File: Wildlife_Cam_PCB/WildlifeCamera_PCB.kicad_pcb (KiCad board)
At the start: 2 copper layers, 79.8 x 84.8 mm, 46 parts, among them J1 PIR, J2 TRIG, J3 RTC_DS3231, J4 PROG, J5 PROG_EN, J6 LOGO1, J7 LOGO2, J8 PCB, Q1 2N3904, Q2 2N3904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

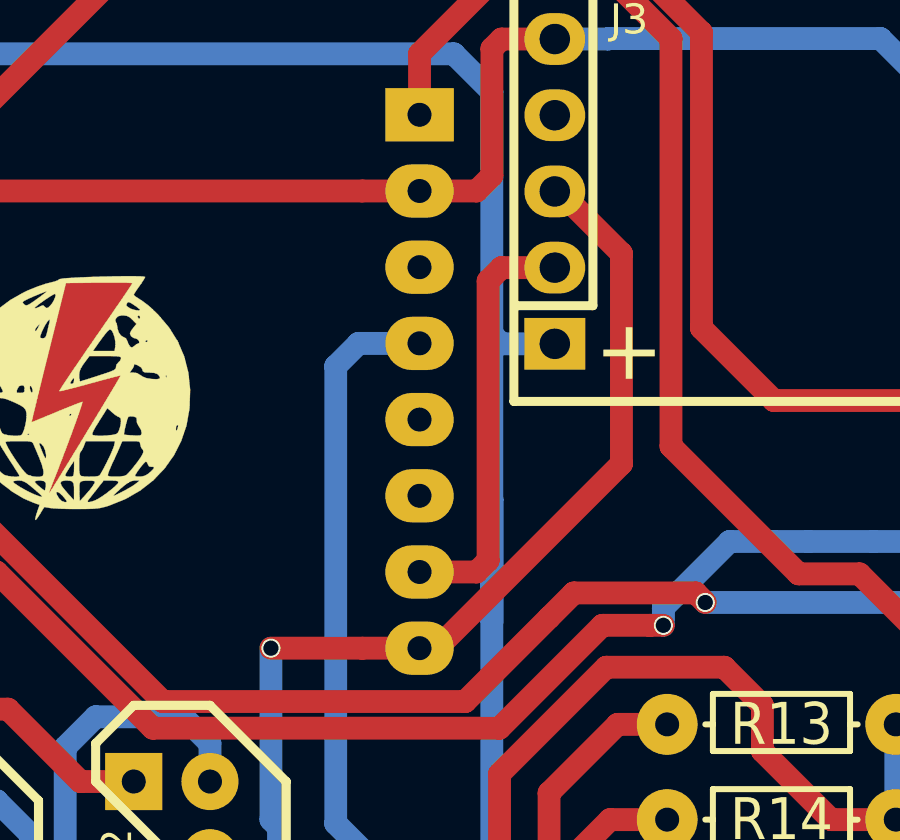
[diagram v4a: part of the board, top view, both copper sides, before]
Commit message: Large update with email sending code
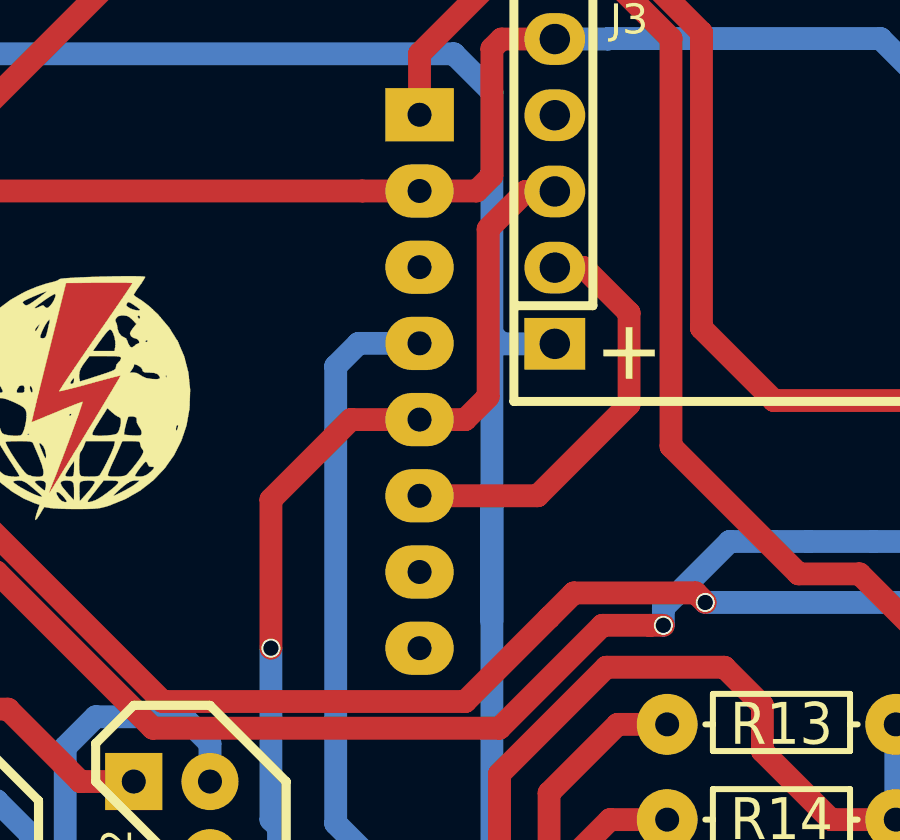
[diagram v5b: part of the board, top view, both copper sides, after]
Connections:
- U3 pad 5: Net-(U3-Pad5) -> /I2C_CLK
- U3 pad 6: Net-(U3-Pad6) -> /I2C_DAT
- U3 pad 7: /I2C_DAT -> Net-(U3-Pad7)
- U3 pad 8: /I2C_CLK -> Net-(U3-Pad8)
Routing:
- net /I2C_CLK: track 46.7 -> 44.4 mm

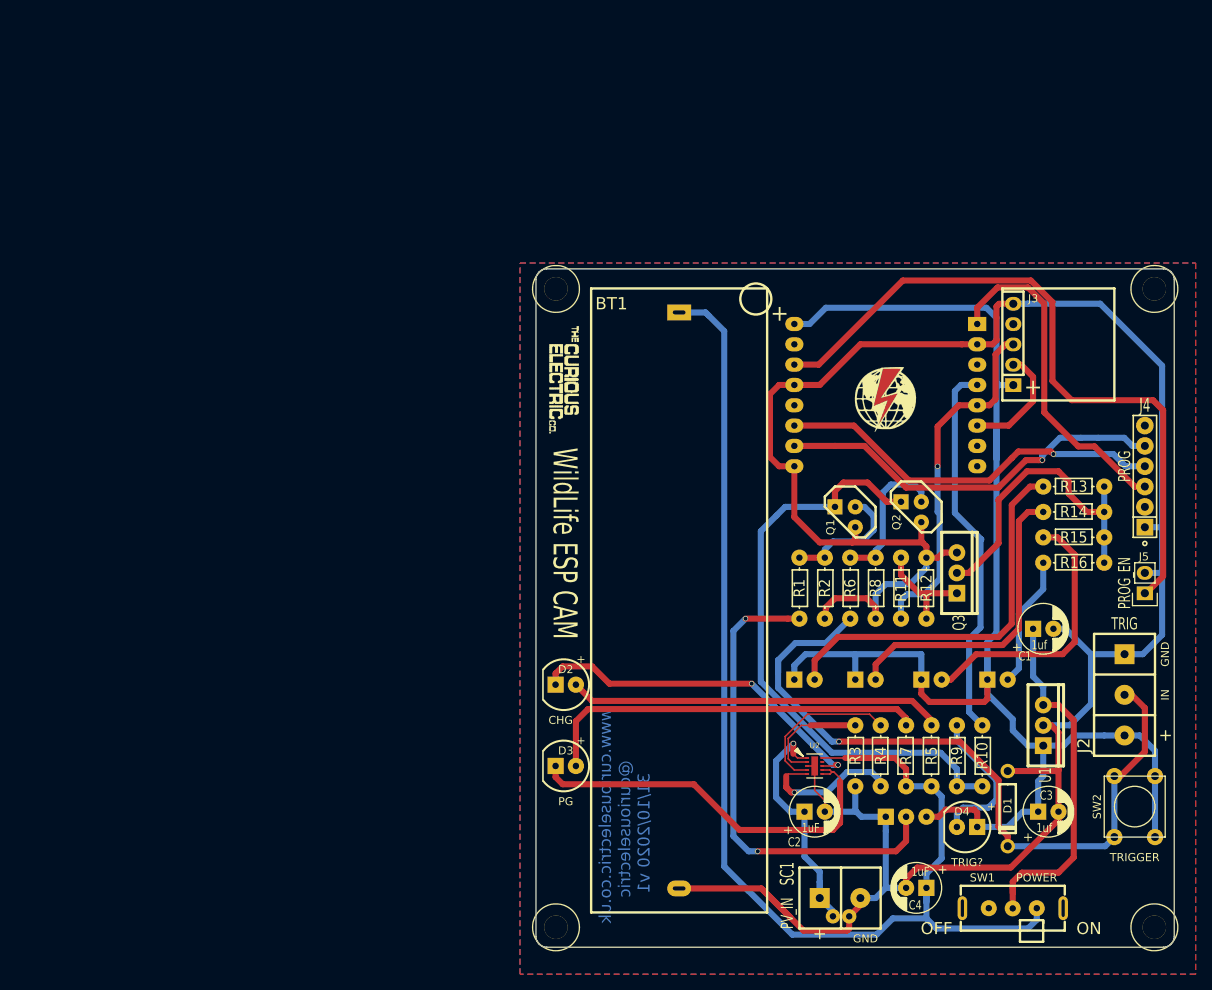
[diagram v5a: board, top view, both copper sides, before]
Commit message: Added new PCB design
Add on for solar charger module. Lapse-O-Matic
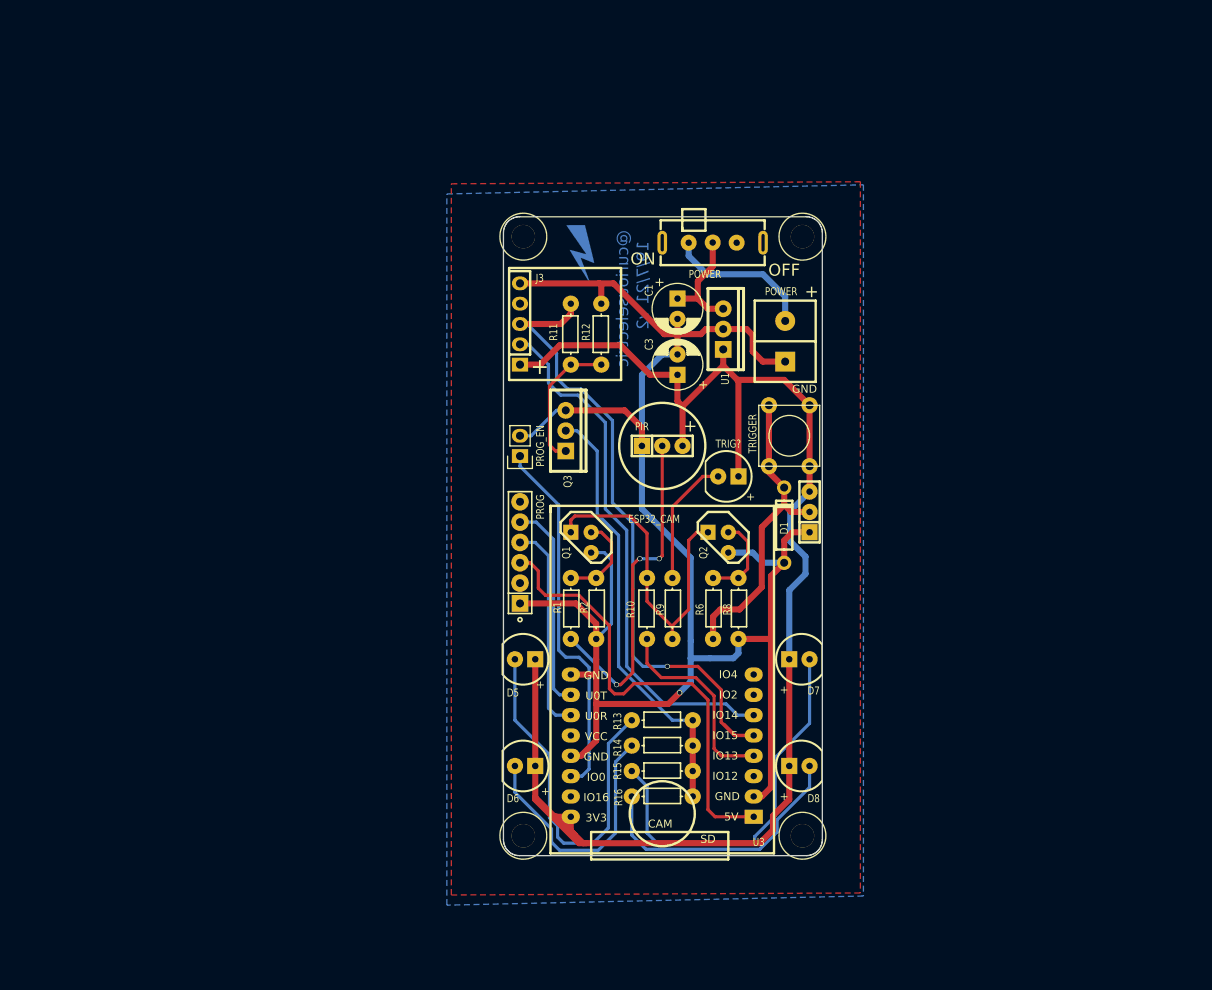
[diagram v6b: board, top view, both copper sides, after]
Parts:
- removed BT1: 18650 LiIon Cell, REInnovationFootprint:TH_LiIon_Holder
- removed C2, C4: 1uF, REInnovationFootprint:C_1V7_TH
- removed D2: CHG, REInnovationFootprint:TH_LED-5MM_larg_pad
- removed D3: PG, REInnovationFootprint:TH_LED-5MM_larg_pad
- removed R3: 1k, REInnovationFootprint:TH_Resistor_1
- removed R4: 100k, REInnovationFootprint:TH_Resistor_1
- removed R5, R7: 2.2k, REInnovationFootprint:TH_Resistor_1
- removed SC1: PV_IN, REInnovationFootprint:SIL_2_screw_+_JST_2mm
- removed U2: BQ24210, REInnovationFootprint:SM_WSON-10-2x3
- added J10: POWER, REInnovationFootprint:SIL-2_screw_terminal, F.Cu at (135.4, 65.0)
- D5, D6, D7, D8, J1, J7: moved to F.Cu
- J2: footprint REInnovationFootprint:SIL-3_screw_terminal -> REInnovationFootprint:SIL-3_lg_pad
- J6, U3: moved to B.Cu
- J8: footprint REInnovationFootprint:PCB_Wildlife_Cam -> REInnovationFootprint:PCB_SolarChargerPCB40x80
- moved J8 97.1 mm to (119.7, 89.6)
- moved SW1 91.3 mm to (126.3, 50.2), turned to 90 degrees
- moved J5 80.0 mm to (102.2, 76.8)
- moved J4 78.7 mm to (102.2, 88.9)
- moved C3 72.6 mm to (121.9, 65.4), turned to 90 degrees
- moved U3 67.6 mm to (120.0, 121.9)
- moved U1 63.7 mm to (127.6, 61.0)
- moved SW2 63.4 mm to (135.9, 74.3)
- moved J3 61.7 mm to (114.9, 53.3)
- moved C1 60.8 mm to (121.9, 58.4), turned to 270 degrees
- moved R13 59.2 mm to (120.0, 109.9)
- moved R14 59.2 mm to (120.0, 113.0)
- moved R15 59.2 mm to (120.0, 116.2)
- moved R16 59.2 mm to (120.0, 119.4)
- moved J1 55.5 mm to (120.0, 75.6)
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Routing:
- net VCC: track 155.9 -> 18.9 mm
- net GND: track 303.6 -> 228.5 mm, vias 0 -> 1
- net Net-(D3-Pad1): track 62.9 -> 0.00 mm
- net Net-(D1-Pad1): track 92.4 -> 38.6 mm, vias 1 -> 0
- net /I2C_DAT: track 14.4 -> 66.0 mm
- net Net-(D3-Pad2): track 48.9 -> 0.00 mm
- net Net-(D2-Pad2): track 46.9 -> 0.00 mm
- net Net-(D2-Pad1): track 44.2 -> 0.00 mm, vias 2 -> 0
- net /PROG_EN: track 86.8 -> 46.3 mm
- net /I2C_CLK: track 44.4 -> 82.9 mm
- net /TRIG: track 76.7 -> 43.7 mm
- net Net-(C1-Pad1): track 44.7 -> 14.0 mm
- net Net-(C2-Pad1): track 30.4 -> 0.00 mm, vias 1 -> 0
- net Net-(Q3-Pad2): track 39.4 -> 64.1 mm
- net /U0T: track 49.3 -> 26.2 mm, vias 1 -> 0
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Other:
- board size 79.8 x 84.8 mm -> 39.9 x 79.9 mm
- board text added: "19/7/21 v2"
- board text added: "LAPSE-O-MATIC"
- board text removed: "31/10/2020 v1"
- board text removed: "FLASH"
- board text removed: "WildLife ESP CAM"

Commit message: Small updates to PCB
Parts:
- removed J10: POWER, REInnovationFootprint:SIL-2_screw_terminal
- added BT1: 18650 LiIon Cell, REInnovationFootprint:TH_LiIon_Holder, F.Cu at (111.1, 55.9)
- added C2: 1uF, REInnovationFootprint:C_1V7_TH, F.Cu at (139.1, 121.3)
- added C4: 1uF, REInnovationFootprint:C_1V7_TH, F.Cu at (151.8, 130.8)
- added D2: CHG, REInnovationFootprint:TH_LED-5MM_larg_pad, F.Cu at (108.0, 105.4)
- added D3: PG, REInnovationFootprint:TH_LED-5MM_larg_pad, F.Cu at (108.0, 115.6)
- added R3: 1k, REInnovationFootprint:TH_Resistor_1, F.Cu at (144.1, 114.3)
- added R4: 100k, REInnovationFootprint:TH_Resistor_1, F.Cu at (147.3, 114.3)
- added R5: 2.2k, REInnovationFootprint:TH_Resistor_1, F.Cu at (153.7, 114.3)
- added R7: 2.2k, REInnovationFootprint:TH_Resistor_1, F.Cu at (150.5, 114.3)
- added SC1: PV_IN, REInnovationFootprint:SIL_2_screw_+_JST_2mm, F.Cu at (139.7, 132.1)
- added U2: BQ24210, REInnovationFootprint:SM_WSON-10-2x3, F.Cu at (139.1, 115.6)
- D5, D6, D7, D8, J1, J7: moved to B.Cu
- J2: footprint REInnovationFootprint:SIL-3_lg_pad -> REInnovationFootprint:SIL-3_screw_terminal
- J6, U3: moved to F.Cu
- J8: footprint REInnovationFootprint:PCB_SolarChargerPCB40x80 -> REInnovationFootprint:PCB_Wildlife_Cam
- moved J8 97.1 mm to (198.8, 146.1)
- moved SW1 91.3 mm to (163.8, 133.3), turned to 270 degrees
- moved J5 80.0 mm to (180.3, 94.0)
- moved J4 78.7 mm to (180.3, 79.4)
- moved C3 72.6 mm to (168.3, 121.3), turned to 0 degrees
- moved U3 67.6 mm to (148.0, 60.3)
- moved U1 63.7 mm to (167.6, 110.5)
- moved SW2 63.4 mm to (179.1, 120.7)
- moved J3 61.7 mm to (176.5, 55.9)
- moved C1 60.8 mm to (167.6, 98.4), turned to 0 degrees
- moved R13 59.2 mm to (171.4, 80.6)
- moved R14 59.2 mm to (171.4, 83.8)
- moved R15 59.2 mm to (171.4, 87.0)
- moved R16 59.2 mm to (171.4, 90.2)
- moved J1 55.5 mm to (150.5, 121.9)
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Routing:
- net VCC: track 18.9 -> 155.9 mm
- net GND: track 228.5 -> 303.6 mm, vias 1 -> 0
- net Net-(D3-Pad1): track 0.00 -> 62.9 mm
- net Net-(D1-Pad1): track 38.6 -> 92.4 mm, vias 0 -> 1
- net /I2C_DAT: track 66.0 -> 14.4 mm
- net Net-(D3-Pad2): track 0.00 -> 48.9 mm
- net Net-(D2-Pad2): track 0.00 -> 46.9 mm
- net Net-(D2-Pad1): track 0.00 -> 44.2 mm, vias 0 -> 2
- net /PROG_EN: track 46.3 -> 86.8 mm
- net /I2C_CLK: track 82.9 -> 44.4 mm
- net /TRIG: track 43.7 -> 76.7 mm
- net Net-(C1-Pad1): track 14.0 -> 44.7 mm
- net Net-(C2-Pad1): track 0.00 -> 30.4 mm, vias 0 -> 1
- net Net-(Q3-Pad2): track 64.1 -> 39.4 mm
- net /U0T: track 26.2 -> 49.3 mm, vias 0 -> 1
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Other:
- board size 39.9 x 79.9 mm -> 79.8 x 84.8 mm
- board text added: "31/10/2020 v1"
- board text added: "FLASH"
- board text added: "WildLife ESP CAM"
- board text removed: "19/7/21 v2"
- board text removed: "LAPSE-O-MATIC"
